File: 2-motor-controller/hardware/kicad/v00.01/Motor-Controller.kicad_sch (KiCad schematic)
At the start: 1 part, among them J1 RF300

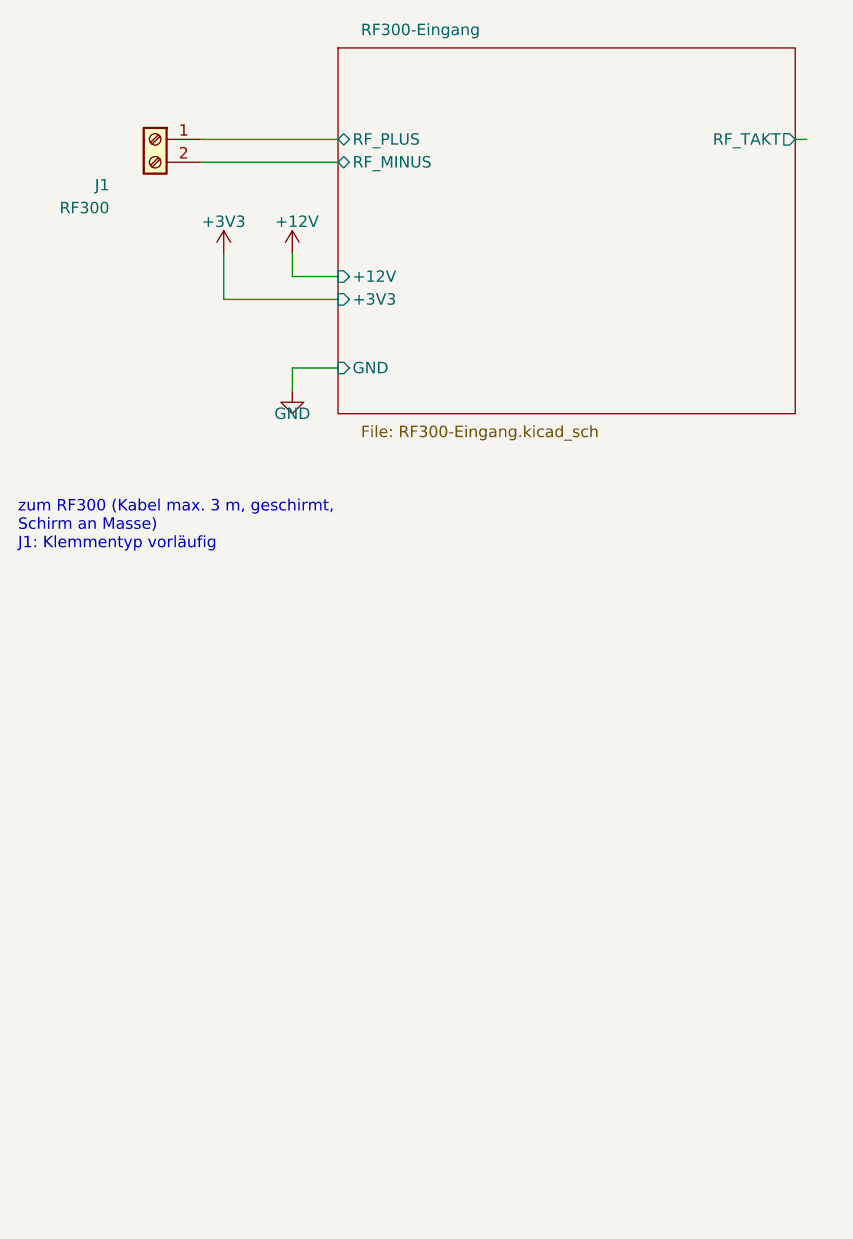
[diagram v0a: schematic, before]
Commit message: Motor-Controller: Unterblatt 5V-Zweig (2x R-78B5.0-2.0), Kabel und Klemmen festgelegt
- Neues Unterblatt 5V-Zweig, im Hauptschaltplan zweimal eingesetzt ("5V Elektronik" -> +5V,
  "5V PyPilot" -> +5V_PYPILOT): Sicherung 2 A mit Leuchtdiode "Sicherung durch", Eingangsfilter
  nach Herstellervorschlag (10 uF - 10 uH - 4,7 uF), Recom R-78B5.0-2.0 (Datenblatt REV 1/2017).
  Bauteilnamen je Zweig 1xx / 2xx.
- Bauteilauswahl 00.05: beide Zweige Recom R-78B5.0-2.0 (Traco verworfen); 5 V zum Steuerstand
  ueber das vorhandene Kabel, Zweig versorgt in Phase 3 auch den SuAnPilot (Festlegung Betreiber);
  Signalklemmen Phoenix MSTBA 2,5 ...-G-5,08 wie auf der RF300-Interfaceplatine.
- Anforderungen 00.04 (F13) und Stueckliste 00.04 entsprechend; J1 auf MSTBA 2,5/2.

Co-Authored-By: Claude Opus 5.5 <noreply@anthropic.com>
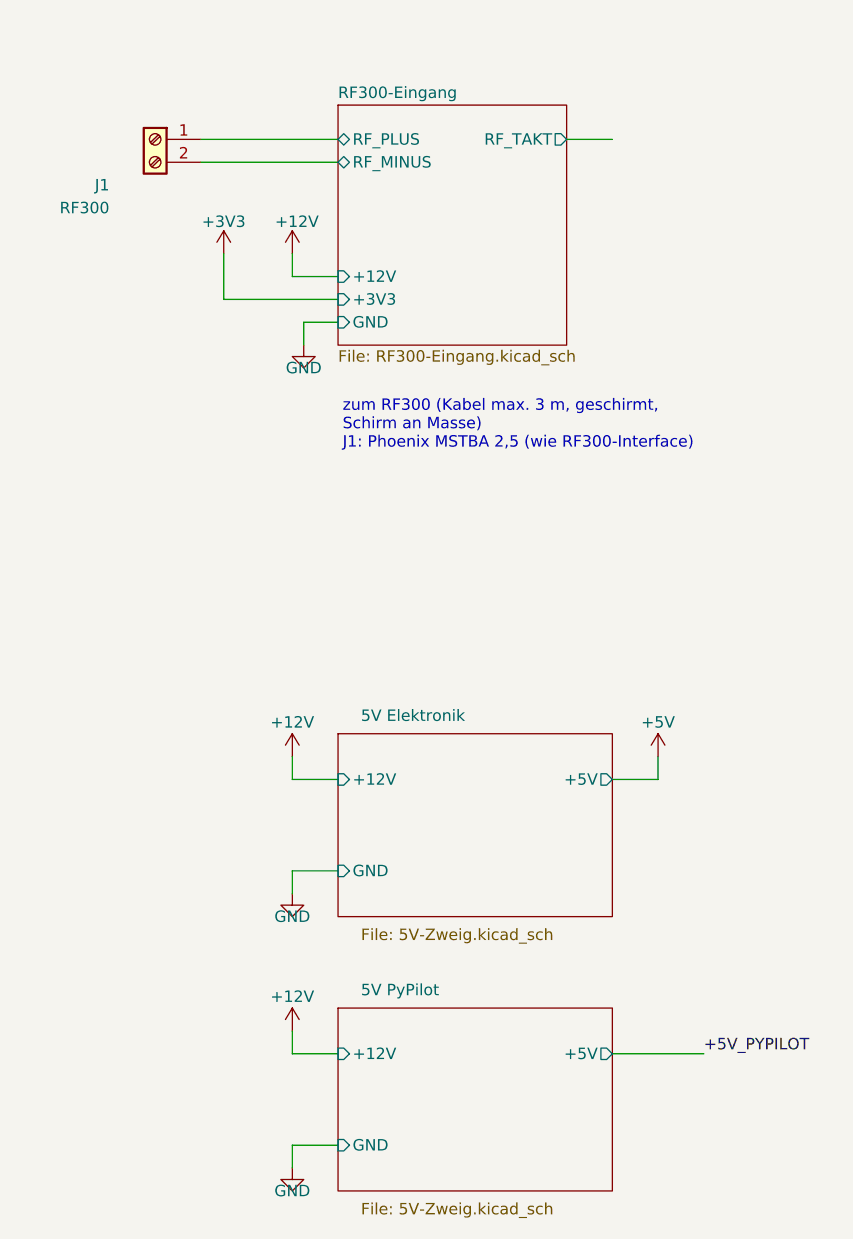
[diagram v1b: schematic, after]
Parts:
- J1: footprint TerminalBlock_Phoenix:TerminalBlock_Phoenix_MKDS-1,5-2-5.08_1x02_P5.08mm_Horizontal -> Connector_Phoenix_MSTB:PhoenixContact_MSTBA_2,5_2-G-5,08_1x02_P5.08mm_Horizontal; Hinweis Klemmentyp vorläufig (Bauteilauswahl Abschnitt 10, Punkt 5) -> Phoenix MSTBA 2,5/2-G-5,08 mit Stecker, wie RF300-Interface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
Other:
- added sheet 5V Elektronik (5V-Zweig.kicad_sch)
- added sheet 5V PyPilot (5V-Zweig.kicad_sch)
- note added: "zum RF300 (Kabel max. 3 m, geschirmt, Schirm an Masse) J1: Phoenix MSTBA 2,5 (wie RF300-Interface)"
- note removed: "zum RF300 (Kabel max. 3 m, geschirmt, Schirm an Masse) J1: Klemmentyp vorläufig"

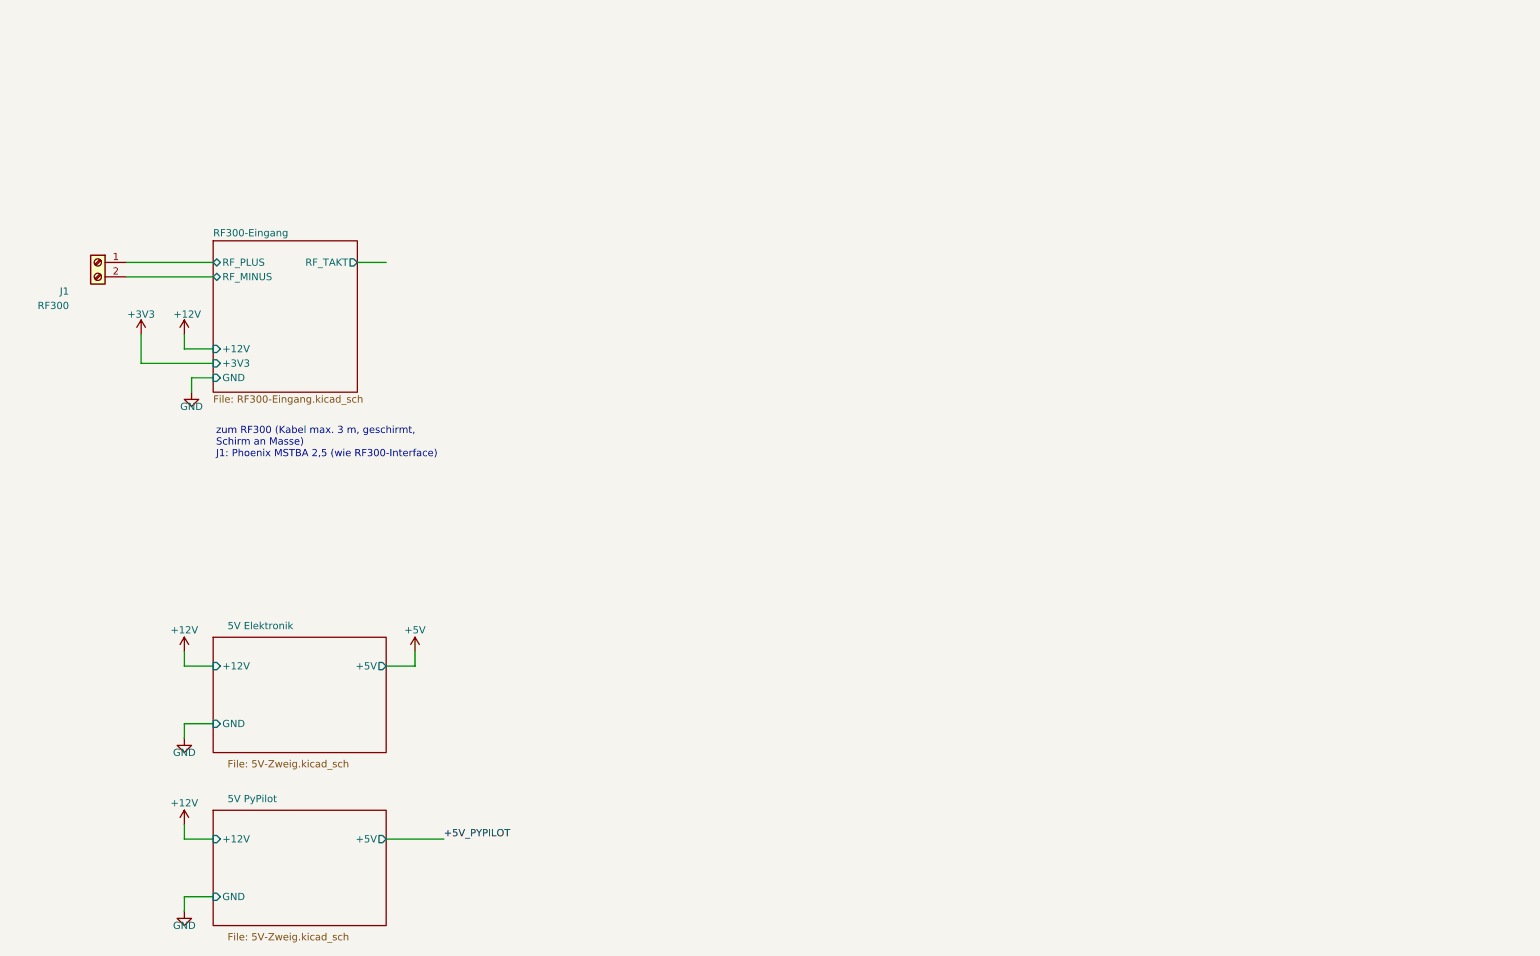
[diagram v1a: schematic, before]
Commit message: Motor-Controller: 12-V-Eingang im Schaltplan; Bauteilauswahl 00.17 / Stueckliste 00.13
- Hauptblatt: Klemme J2, Schutzdiode 1.5KE20A, Elko 1000 uF, Verpolschutz SB540,
  Hinweis zur Verdrahtung des Pololu G2 (Stehbolzen, Buchsenleiste, Messleitungen A/B)
- Keine eigene 20-A-Sicherung (im Schiff vorhanden), Halter gestrichen
- Strommessung: eingebaute Messung des G2; Hall-Sensor ACS758 vorbereitet, nicht bestueckt, 5 V
- Anzeige festgelegt: Grafik-LCD 128x64 ST7920, sieben Leuchtdioden, Warnausgang ohne Summer
- Recom-Datenblatt REV 5/2021; CLAUDE.md: Ablage der Datenblaetter

Co-Authored-By: Claude Opus 5.5 <noreply@anthropic.com>
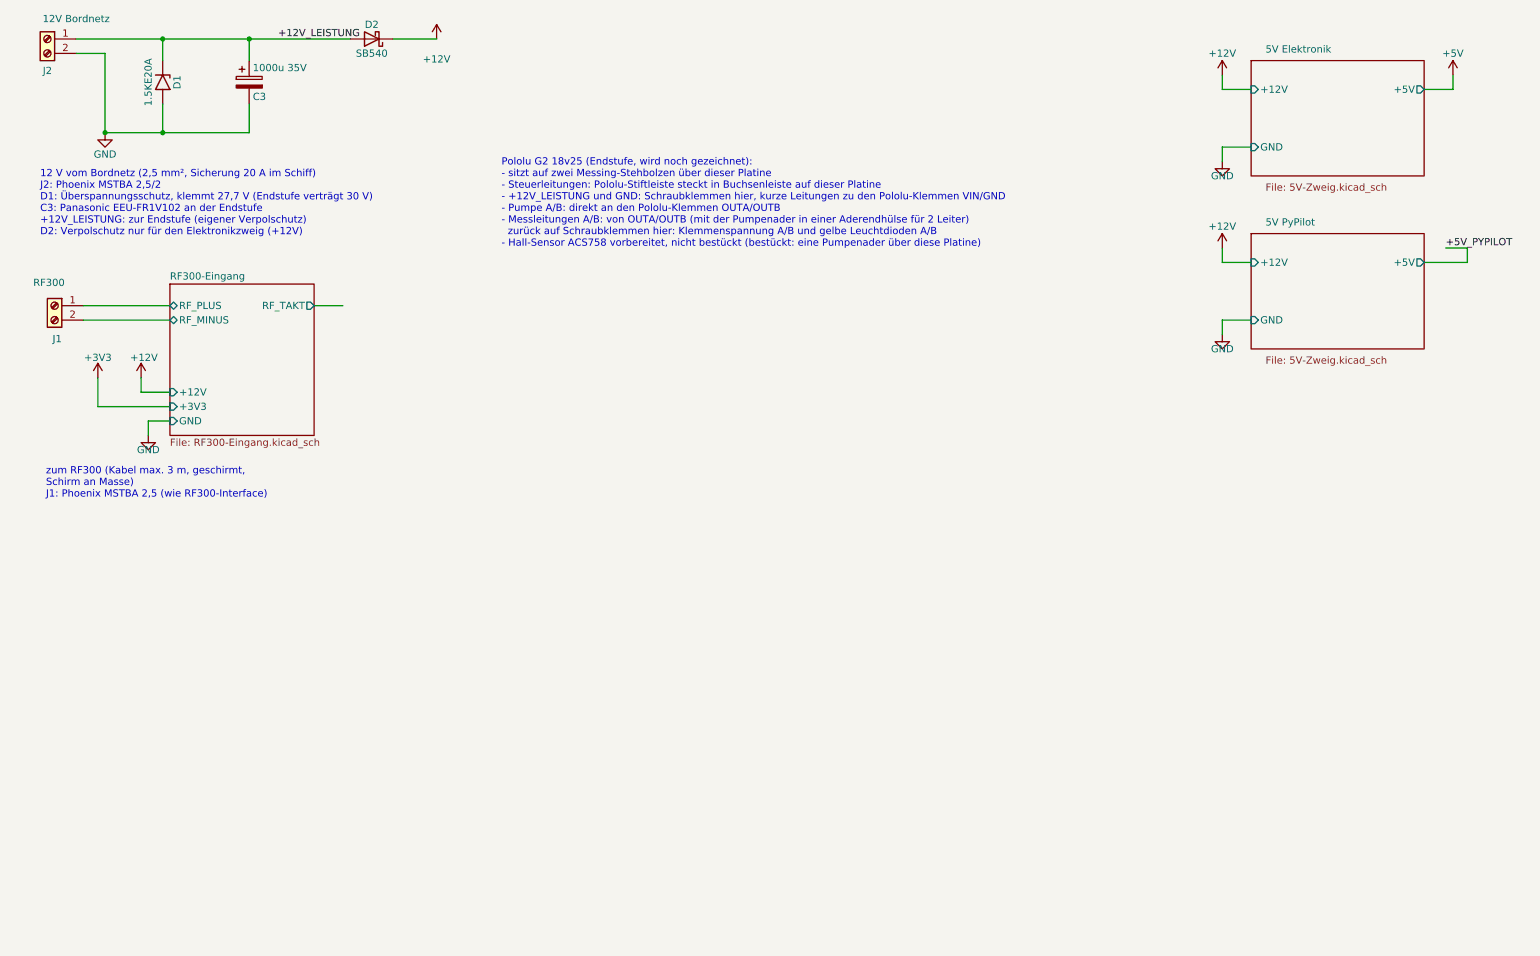
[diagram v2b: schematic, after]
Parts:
- added C3: 1000u 35V, Capacitor_THT:CP_Radial_D12.5mm_P5.00mm, symbol Device:C_Polarized
- added D1: 1.5KE20A, Diode_THT:D_DO-201AE_P15.24mm_Horizontal, symbol Diode:1.5KExxA
- added D2: SB540, Diode_THT:D_DO-201AD_P15.24mm_Horizontal, symbol Device:D_Schottky
- added J2: 12V Bordnetz, Connector_Phoenix_MSTB:PhoenixContact_MSTBA_2,5_2-G-5,08_1x02_P5.08mm_Horizontal, symbol Connector:Screw_Terminal_01x02
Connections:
- net +12V: now also D2.1 (K)
- net GND: now also C3.2, D1.2 (A2), J2.2 (Pin_2)
- new net +12V_LEISTUNG: C3.1, D1.1 (A1), D2.2 (A), J2.1 (Pin_1)
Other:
- note added: "12 V vom Bordnetz (2,5 mm², Sicherung 20 A im Schiff) J2: Phoenix MSTBA 2,5/2 D1: Überspannungsschutz, klemmt 27,7 V (Endstufe verträgt 30 V) C3: Panasonic EEU-FR1V102 an der Endstufe +12V_LEISTUNG: zur Endstufe (eigener Verpolschutz) D2: Verpolschutz nur für den Elektronikzweig (+12V)"
- note added: "Pololu G2 18v25 (Endstufe, wird noch gezeichnet): - sitzt auf zwei Messing-Stehbolzen über dieser Platine - Steuerleitungen: Pololu-Stiftleiste steckt in Buchsenleiste auf dieser Platine - +12V_LEISTUNG und GND: Schraubklemmen hier, kurze Leitungen zu den Pololu-Klemmen VIN/GND - Pumpe A/B: direkt an den Pololu-Klemmen OUTA/OUTB - Messleitungen A/B: von OUTA/OUTB (mit der Pumpenader in einer Ader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"
- moved on the sheet: J1
